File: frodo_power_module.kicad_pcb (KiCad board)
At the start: 2 copper layers, 91.1 x 72.6 mm, 76 parts, among them J1 Keystone 1048, J10 SWD Header, J2 Molex MicroFit 2x3, J3 Molex MicroFit 2x2, J4 Molex MicroFit 2x2, J5 JST-GH, J6 JST-GH, J7 Molex MicroFit 2x3, U1 STM32F042F6Px, U2 L7805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

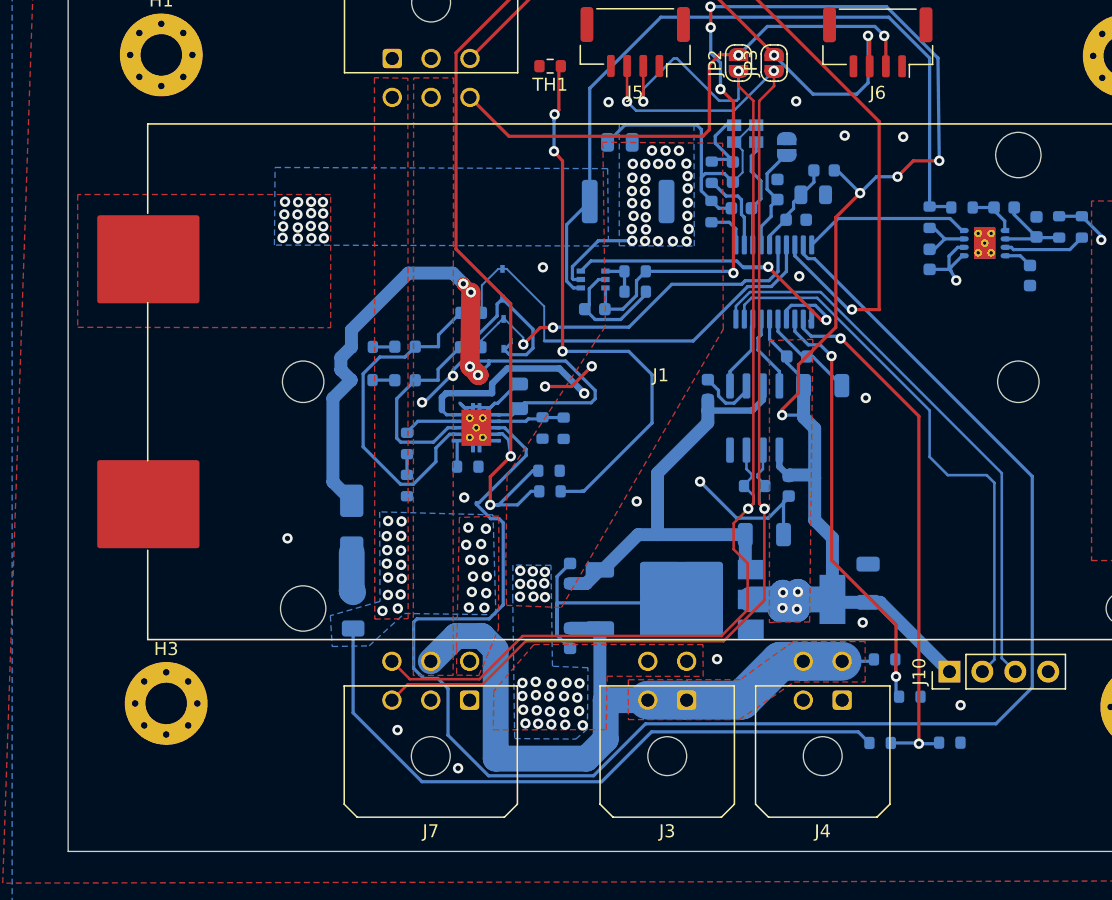
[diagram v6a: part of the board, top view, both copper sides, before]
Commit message: DRC check for hole to hole clerance and minimum trace to trace clearance also changed a few traces and zones
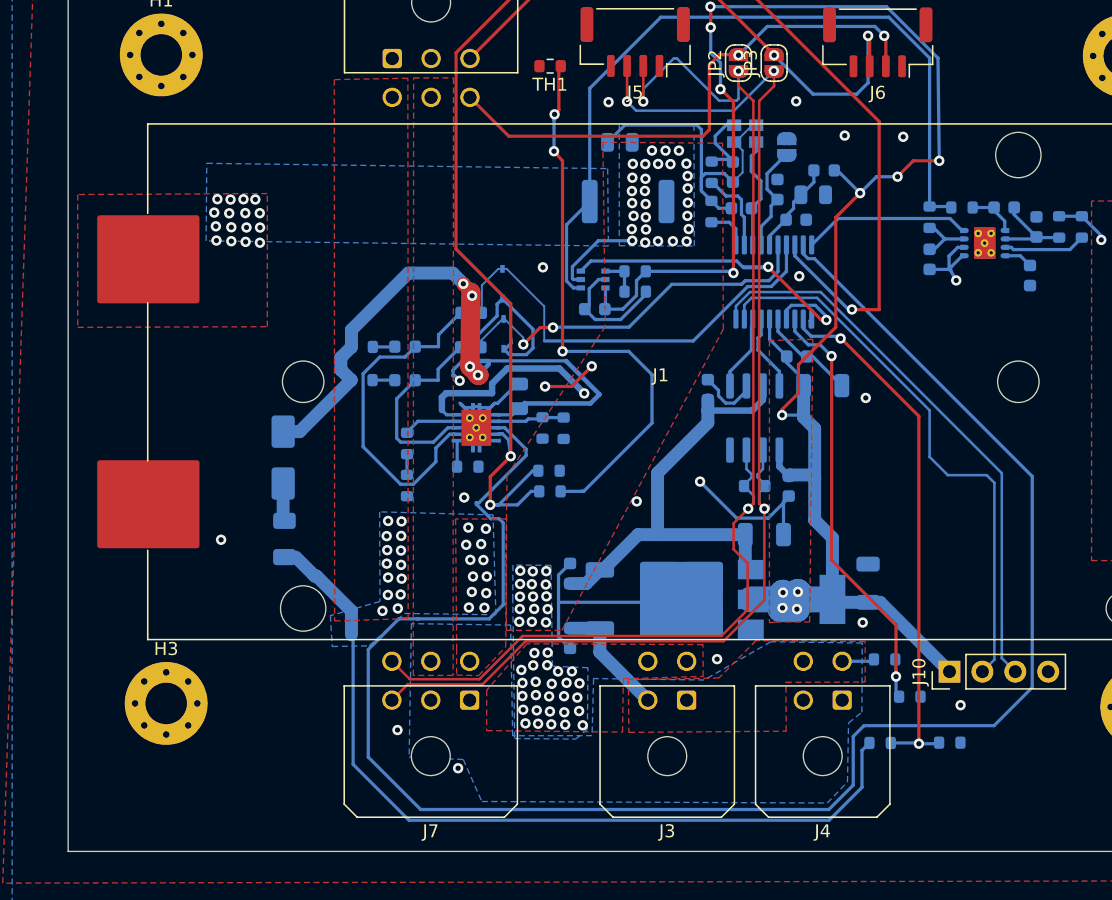
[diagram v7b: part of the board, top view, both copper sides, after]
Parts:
- moved F1 7.65 mm to (95.5, 92.1)
- moved D1 7.51 mm to (95.4, 85.8)
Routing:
- net +VSW: track 56.2 -> 11.9 mm
- net VDC: track 50.5 -> 64.6 mm
- net CHARGE_ENABLE: track 126.9 -> 139.1 mm
- net GND: track 118.2 -> 113.4 mm, vias 21 -> 20
- net Net-(D1-K): track 55.5 -> 52.2 mm
- net +BATT: vias 58 -> 71
- added copper zone on B.Cu, net +VSW
